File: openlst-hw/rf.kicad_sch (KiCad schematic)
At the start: 40 parts, among them J5 SMA Jack, J6 Conn_01x03_Pin, J7 SMA Jack, U3 SF2446E, U4 PE4250MLI, U5 PE4250MLI, U6 0433BM15A0001, U7 RFFM6406

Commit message: propate the changes to RF
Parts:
- C15, C16, C23, C24, C25, C26, C27, C28, C29, C30, C37, C38: Order https://www.digikey.com/product-detail/en/samsung-electro-m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 -> (none)
- C17, C18, C20, C21: Order https://www.digikey.com/product-detail/en/murata-electronic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 -> (none)
- C19, C22: Order https://www.digikey.com/product-detail/en/tdk-corporation/C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 -> (none)
- FB2, FB3, FB4: Order https://www.digikey.com/en/products/detail/murata-electroni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 -> (none)
- J5, J7: Order https://www.digikey.com/en/products/detail/amphenol-rf/901-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 -> (none)
- J6: Part Number (none) -> generic; now fitted
- R16, R17, R18, R19, R20: Order https://www.digikey.com/en/products/detail/stackpole-electr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 -> (none)
- U3: Order https://www.digikey.com/en/products/detail/rfmi/SF2446E/121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 -> (none)
- U4, U5: Order https://www.digikey.com/en/products/detail/psemi/PE4250MLI-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 -> (none)
- U6: Order https://www.digikey.com/en/products/detail/johanson-technol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 -> (none)
- U7: Order https://www.mouser.com/ProductDetail/772-RFFM6406SR -> (none)

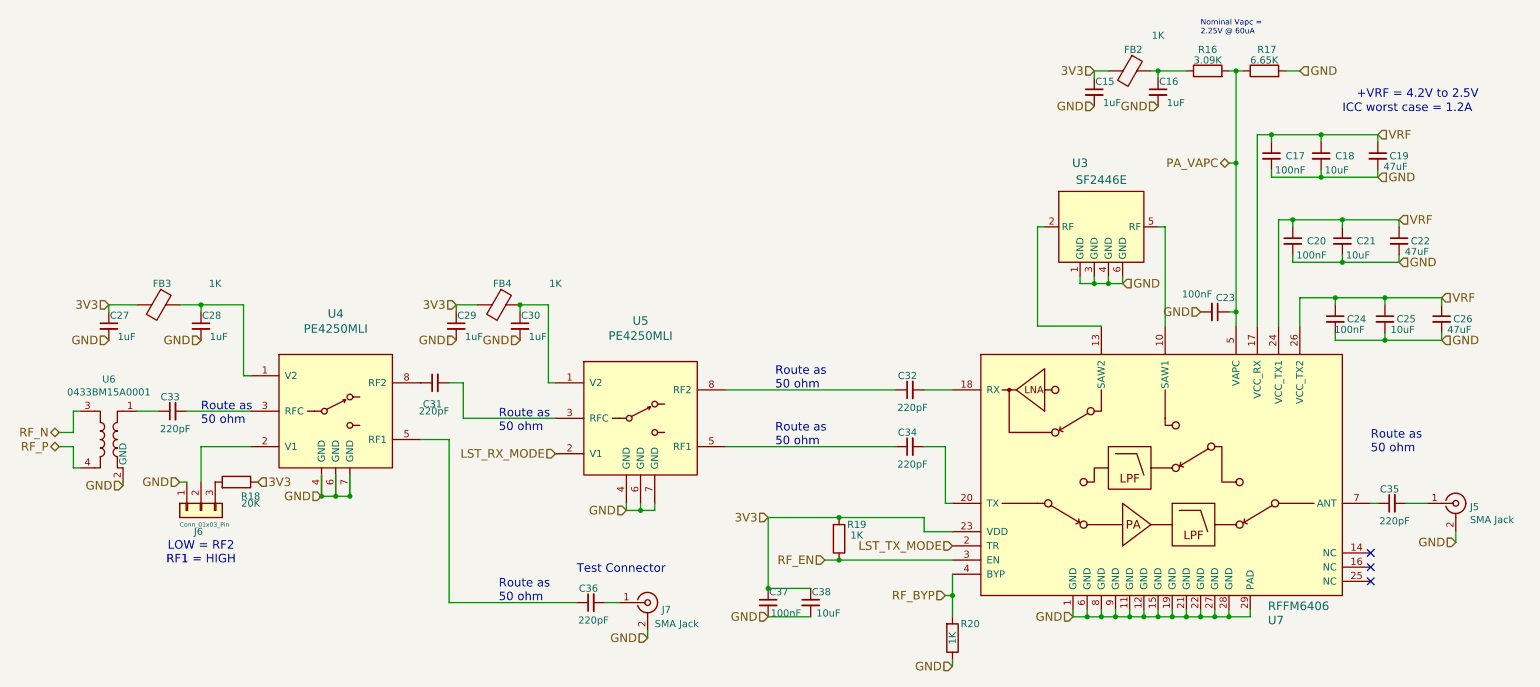
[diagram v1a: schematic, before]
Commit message: local switches and monitors for SCI and RF
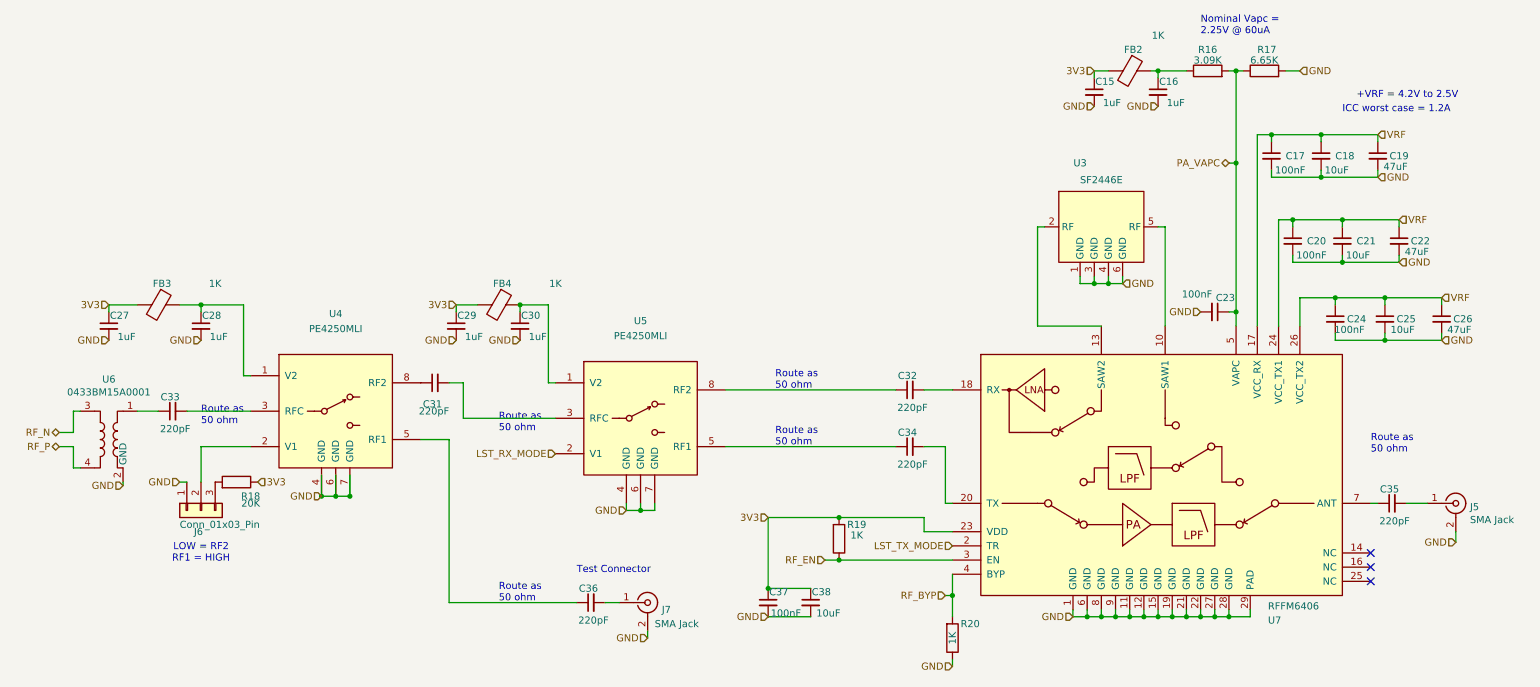
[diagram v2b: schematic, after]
